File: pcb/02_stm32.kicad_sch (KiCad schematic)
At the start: 23 parts, among them SW4 RESET, U17 STM32F407VET6, X3 8MHz CL=12pF

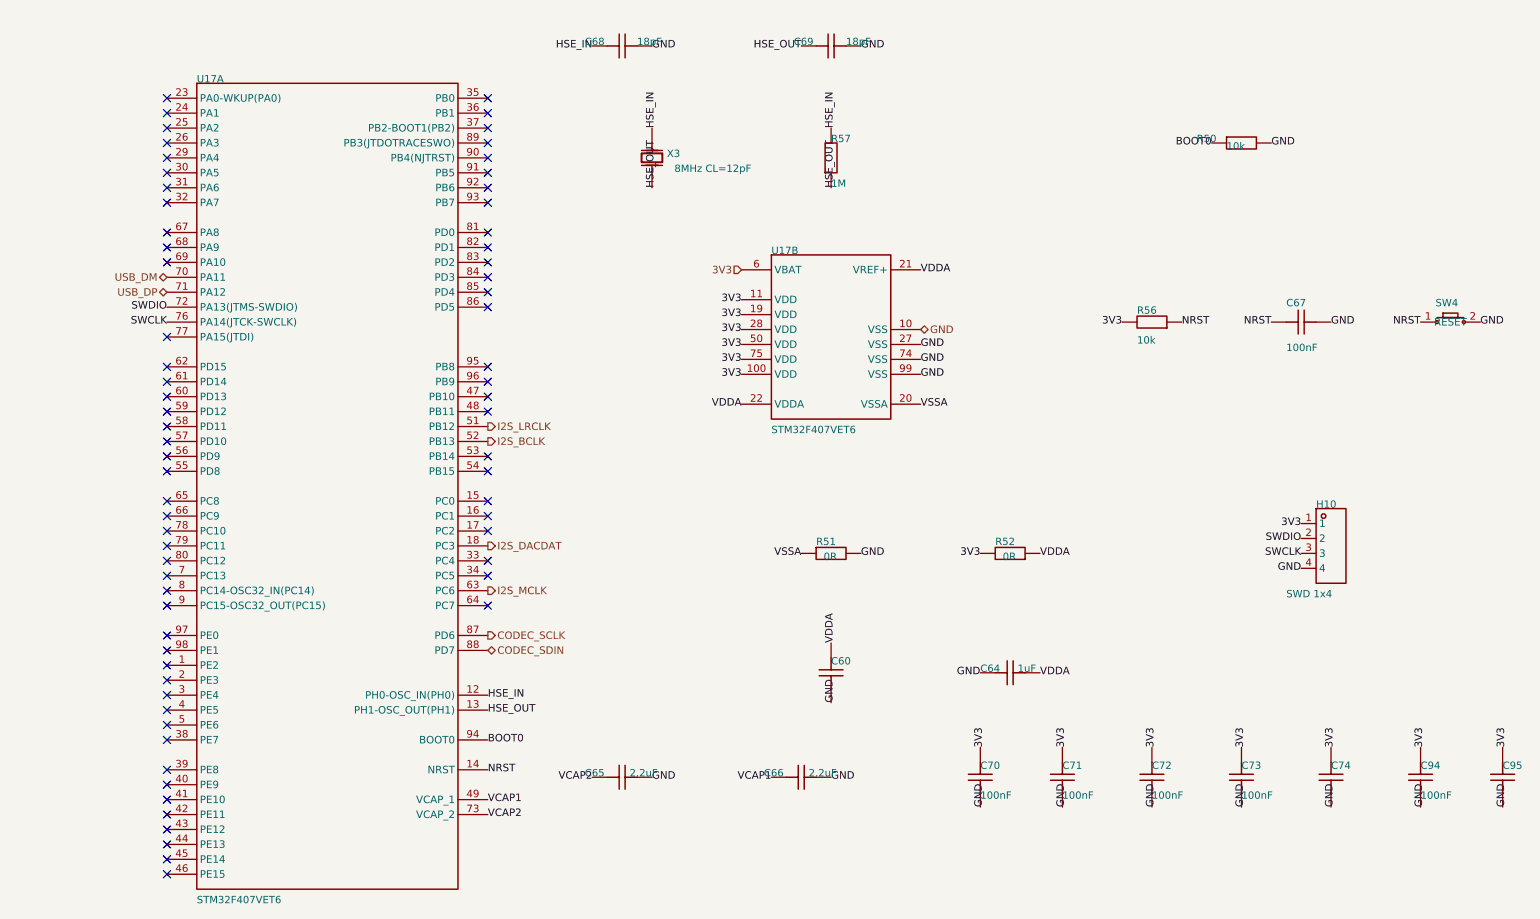
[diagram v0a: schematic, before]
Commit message: 修复原理图电源网络并更新项目文档
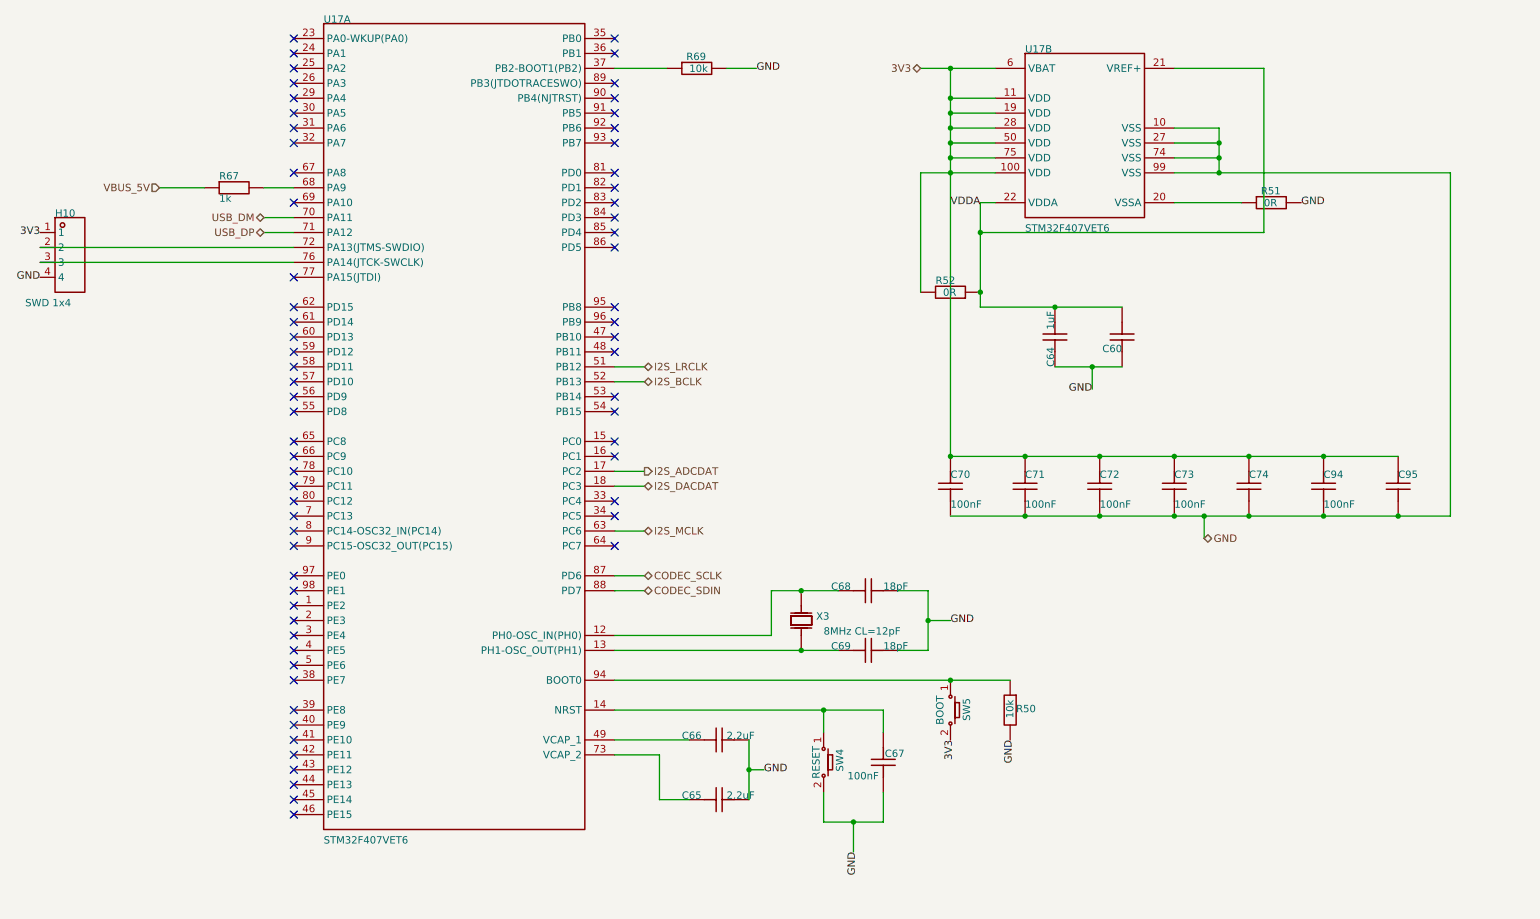
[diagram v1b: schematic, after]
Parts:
- removed R56: 10k, Resistor_SMD:R_0603_1608Metric, symbol WM8978-easyedapro:电阻
- removed R57: 1M, Resistor_SMD:R_0603_1608Metric, symbol WM8978-easyedapro:电阻
- added R67: 1k, Resistor_SMD:R_0603_1608Metric, symbol WM8978-easyedapro:电阻
- added R69: 10k, Resistor_SMD:R_0603_1608Metric, symbol WM8978-easyedapro:电阻
- added SW5: BOOT, Button_Switch_SMD:SW_SPST_TL3342, symbol WM8978-easyedapro:轻触按键x2
- C95: footprint Capacitor_SMD:C_0805_2012Metric -> Capacitor_SMD:C_0603_1608Metric
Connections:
- net 3V3: now also SW5.2
- net GND: now also C60.1, R69.2; no longer C60.2
- net VDDA: now also C60.2; no longer C60.1
- net I2S_ADCDAT: now reaches U17.17 (PC2)
- net at U17.37 (PB2-BOOT1(PB2)): now also R69.1
- net at U17.68 (PA9): now also R67.2
- net BOOT0: no longer names the net of R50.1, U17.94 (BOOT0)
- net BOOT0: now also SW5.1
- net HSE_IN: no longer names the net of C68.1, U17.12 (PH0-OSC_IN(PH0)), X3.2 (OSC2)
- net HSE_OUT: no longer names the net of C69.1, U17.13 (PH1-OSC_OUT(PH1)), X3.1 (OSC1)
- net NRST: no longer names the net of C67.2, SW4.1, U17.14 (NRST)
- net SWCLK: no longer names the net of H10.3, U17.76 (PA14(JTCK-SWCLK))
- net SWDIO: no longer names the net of H10.2, U17.72 (PA13(JTMS-SWDIO))
- net VCAP1: no longer names the net of C66.1, U17.49 (VCAP_1)
- net VCAP2: no longer names the net of C65.1, U17.73 (VCAP_2)
- net VSSA: no longer names the net of R51.1, U17.20 (VSSA)
- new net VBUS_5V: R67.1
- no-connect marks 70 -> 67
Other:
- title: STM32F407 Core, Clock and Debug -> STM32F407 USB FS and Full-Duplex I2S
- moved on the sheet: C65, C66, C67, C68, C69, C70, C71, C72, C73, C74, C94, C95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
